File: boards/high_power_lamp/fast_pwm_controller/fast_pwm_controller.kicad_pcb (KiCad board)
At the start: 2 copper layers, 72 x 72 mm, 102 parts, among them J1 Screw_Terminal_01x01, J10 Screw_Terminal_01x01, J11 Screw_Terminal_01x01, J12 Screw_Terminal_01x01, J13 Screw_Terminal_01x01, J14 Screw_Terminal_01x01, J15 Screw_Terminal_01x01, J16 Screw_Terminal_01x01, J17 Screw_Terminal_01x01, J18 Screw_Terminal_01x01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

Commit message: finalise pcb
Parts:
- moved J5 33.0 mm to (95.0, 110.5)
- moved J3 22.0 mm to (62.0, 110.5)
- moved J7 22.0 mm to (73.0, 110.5)
- moved TP10 20.3 mm to (71.1, 68.3)
- moved J9 11.0 mm to (84.0, 110.5)
- moved TP8 9.47 mm to (68.9, 59.1)
- moved R21 5.65 mm to (88.6, 96.8), turned to -90 degrees
- moved R18 4.86 mm to (69.5, 103.2)
- moved R24 4.86 mm to (74.0, 103.2)
- moved TP6 4.42 mm to (91.1, 65.1)
- moved TP4 3.62 mm to (93.0, 61.9)
- moved U2 3.44 mm to (81.0, 63.2), turned to 0 degrees
- moved C2 2.42 mm to (74.0, 72.4), turned to -90 degrees
- moved TP2 1.31 mm to (88.9, 70.5)
- moved R11 0.95 mm to (88.6, 101.3)
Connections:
- C16 pad 2: Net-(U2C-+) -> Net-(U2B-+)
- C17 pad 2: Net-(U2B-+) -> Net-(U2D-+)
- C8 pad 2: Net-(U2D-+) -> Net-(U2C-+)
- J14 pad 1: /PWM stage 2/OUT -> /PWM stage 4/OUT
- J16 pad 1: /PWM stage 3/OUT -> /PWM stage 2/OUT
- J18 pad 1: /PWM stage 4/OUT -> /PWM stage 3/OUT
- J5 pad 1: /PWM stage 2/IN -> /PWM stage 4/IN
- J7 pad 1: /PWM stage 3/IN -> /PWM stage 2/IN
- J9 pad 1: /PWM stage 4/IN -> /PWM stage 3/IN
- JP1 pad 1: /PWM stage 1/IN -> /PWM stage 3/IN
- JP3 pad 1: /PWM stage 2/IN -> /PWM stage 1/IN
- JP4 pad 1: /PWM stage 3/IN -> /PWM stage 4/IN
- JP5 pad 1: /PWM stage 4/IN -> /PWM stage 2/IN
- Q2 pad 2: /PWM stage 2/OUT -> /PWM stage 4/OUT
- Q3 pad 2: /PWM stage 3/OUT -> /PWM stage 2/OUT
- Q4 pad 2: /PWM stage 4/OUT -> /PWM stage 3/OUT
- R11 pad 1: /PWM stage 1/IN -> /PWM stage 3/IN
- R12 pad 1: Net-(U2D-+) -> Net-(U2C-+)
- R18 pad 1: /PWM stage 2/IN -> /PWM stage 1/IN
- R19 pad 1: Net-(U2C-+) -> Net-(U2B-+)
- R21 pad 1: /PWM stage 3/IN -> /PWM stage 4/IN
- R22 pad 1: Net-(U2B-+) -> Net-(U2D-+)
- R24 pad 1: /PWM stage 4/IN -> /PWM stage 2/IN
- TP10 pad 1: Net-(R26-Pad2) -> Net-(R23-Pad2)
- TP3 pad 1: Net-(U2D-+) -> Net-(U2C-+)
- TP4 pad 1: Net-(R13-Pad2) -> Net-(R20-Pad2)
- TP5 pad 1: Net-(U2C-+) -> Net-(U2B-+)
- TP6 pad 1: Net-(R20-Pad2) -> Net-(R26-Pad2)
- TP7 pad 1: Net-(U2B-+) -> Net-(U2D-+)
- TP8 pad 1: Net-(R23-Pad2) -> Net-(R13-Pad2)
- U1 pad 3: /PWM stage 2/IN -> /PWM stage 1/IN
- U1 pad 5: /PWM stage 4/IN -> /PWM stage 2/IN
- U1 pad 7: /PWM stage 1/IN -> /PWM stage 3/IN
- U1 pad 9: /PWM stage 3/IN -> /PWM stage 4/IN
- U2 pad 1: Net-(R23-Pad2) -> Net-(R13-Pad2)
- U2 pad 10: /PWM stage 2/TRIANGLE -> /PWM stage 1/TRIANGLE
- U2 pad 13: Net-(R20-Pad2) -> Net-(R26-Pad2)
- U2 pad 14: Net-(R13-Pad2) -> Net-(R20-Pad2)
- U2 pad 2: Net-(R26-Pad2) -> Net-(R23-Pad2)
- U2 pad 8: /PWM stage 1/TRIANGLE -> /PWM stage 2/TRIANGLE
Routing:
- net /PWM stage 2/OUT: track 19.4 -> 49.9 mm
- net /PWM stage 4/OUT: track 42.2 -> 19.4 mm
- net Net-(R13-Pad2): track 40.1 -> 27.8 mm
- net /PWM stage 3/IN: track 26.8 -> 15.0 mm
- net /PWM stage 1/IN: track 14.9 -> 26.1 mm
- net /PWM stage 2/IN: track 28.3 -> 20.5 mm
- net /PWM stage 3/OUT: track 49.9 -> 42.2 mm
- net Net-(R20-Pad2): track 32.0 -> 24.7 mm
- net Net-(U2A-+): track 21.2 -> 28.1 mm, vias 0 -> 1
- net Net-(R26-Pad2): track 39.5 -> 33.9 mm
- net GND: track 20.3 -> 15.2 mm, vias 83 -> 91
- net Net-(U2B-+): track 20.1 -> 24.8 mm, vias 0 -> 1
- net +12V: track 100.3 -> 104.4 mm
- net /PWM stage 2/TRIANGLE: track 23.3 -> 26.1 mm, vias 3 -> 0
- net VPP: track 69.7 -> 71.7 mm
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
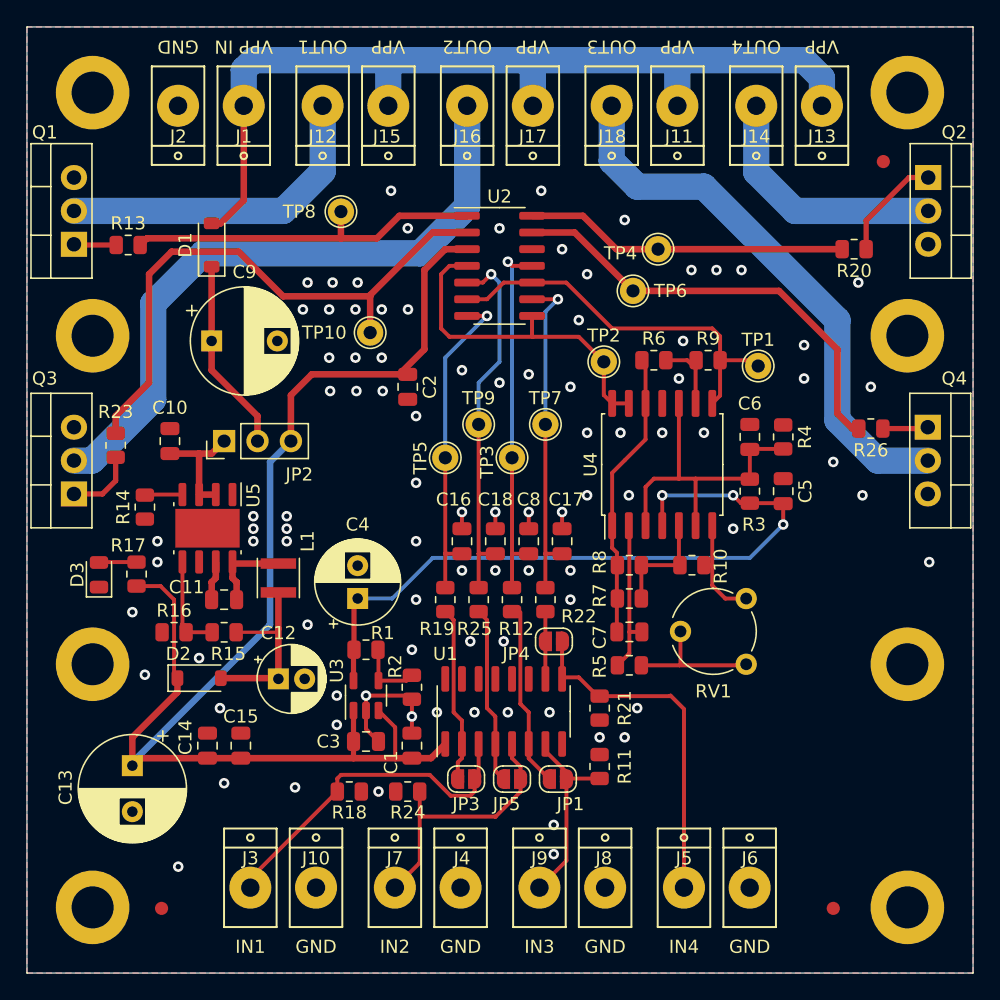
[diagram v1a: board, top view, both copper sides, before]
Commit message: final touches to the fast pwm controller
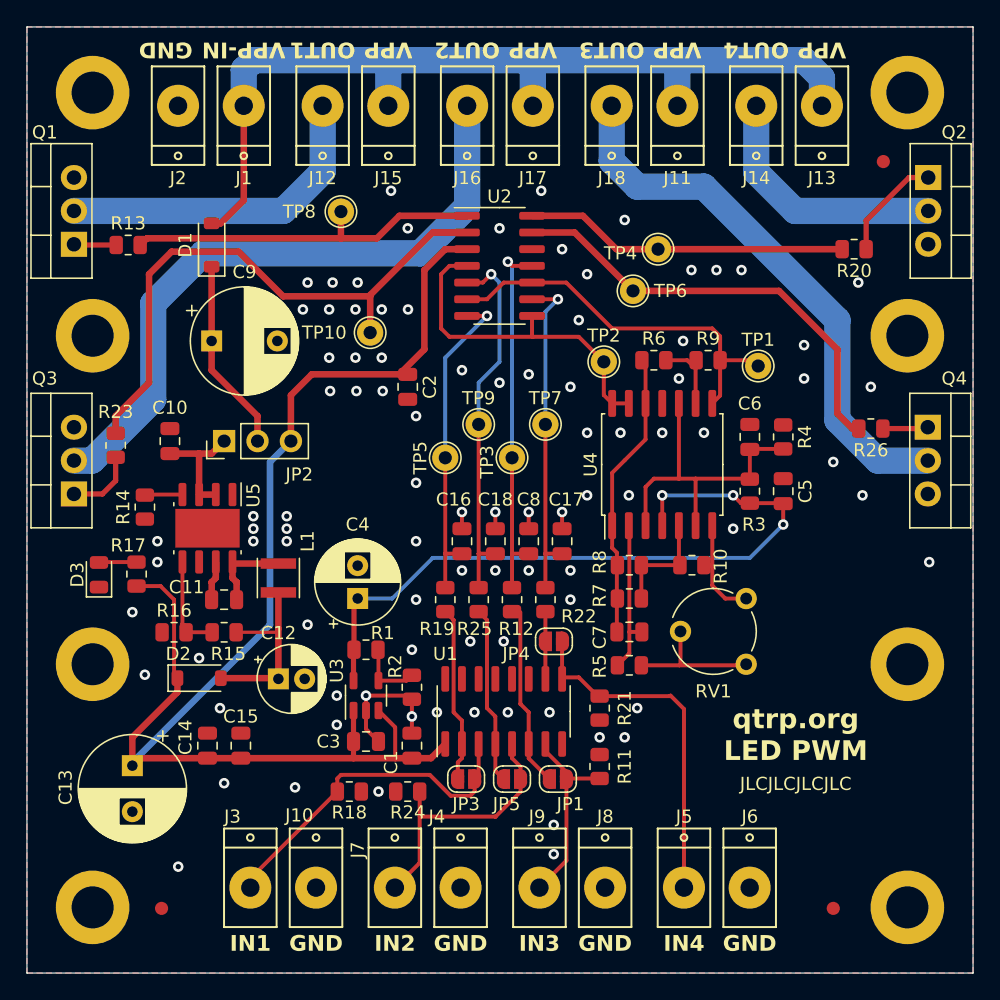
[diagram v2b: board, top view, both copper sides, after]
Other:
- board text added: "JLCJLCJLCJLC"
- board text added: "qtrp.org LED PWM"
